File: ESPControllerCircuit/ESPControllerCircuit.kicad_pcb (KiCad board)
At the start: 2 copper layers, 75 x 30 mm, 25 parts, among them J1 Input, J2 Input, J3 Input, J4 Input, J5 Optional, U1 WeMos_mini, U2 HMHA2801, U3 PCF8574T/3,518

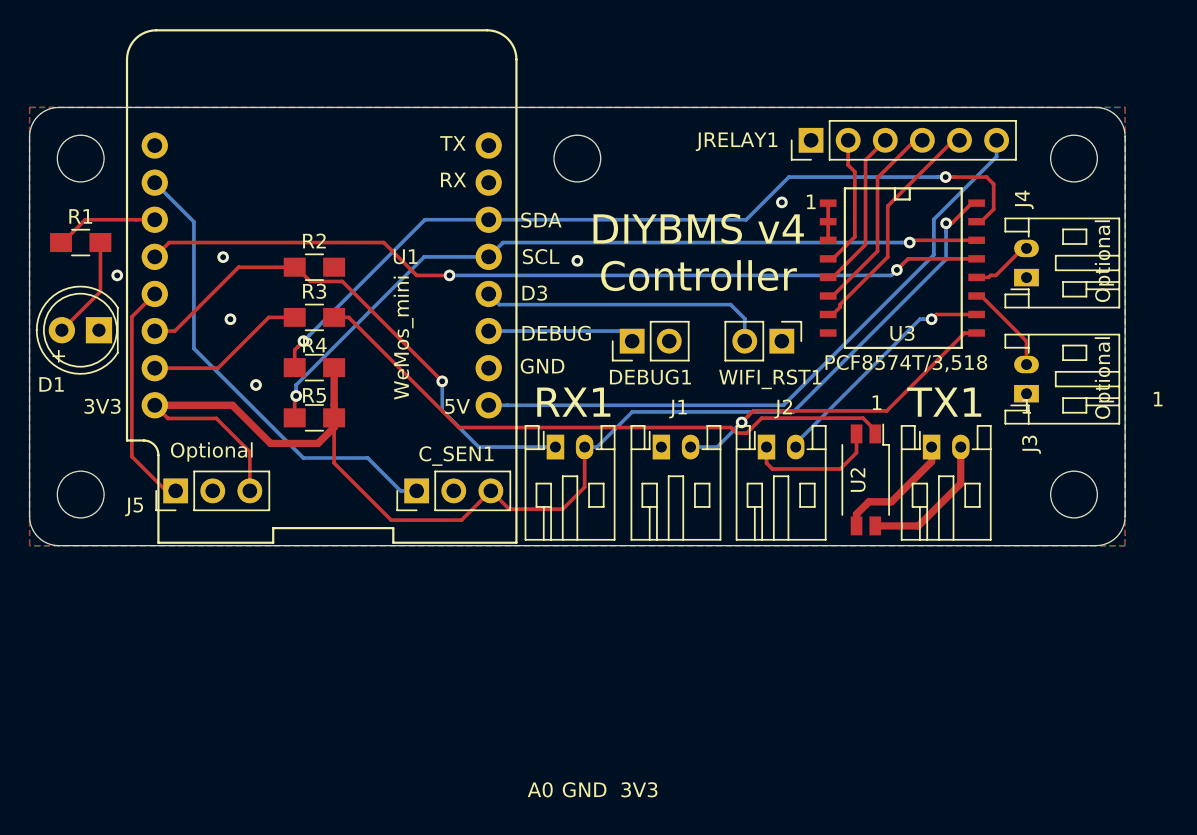
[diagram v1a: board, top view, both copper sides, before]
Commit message: Fix for issue #44
Enlarge footprint for PCF8574 to SOIC16-Wide
Swap LED to surface mount
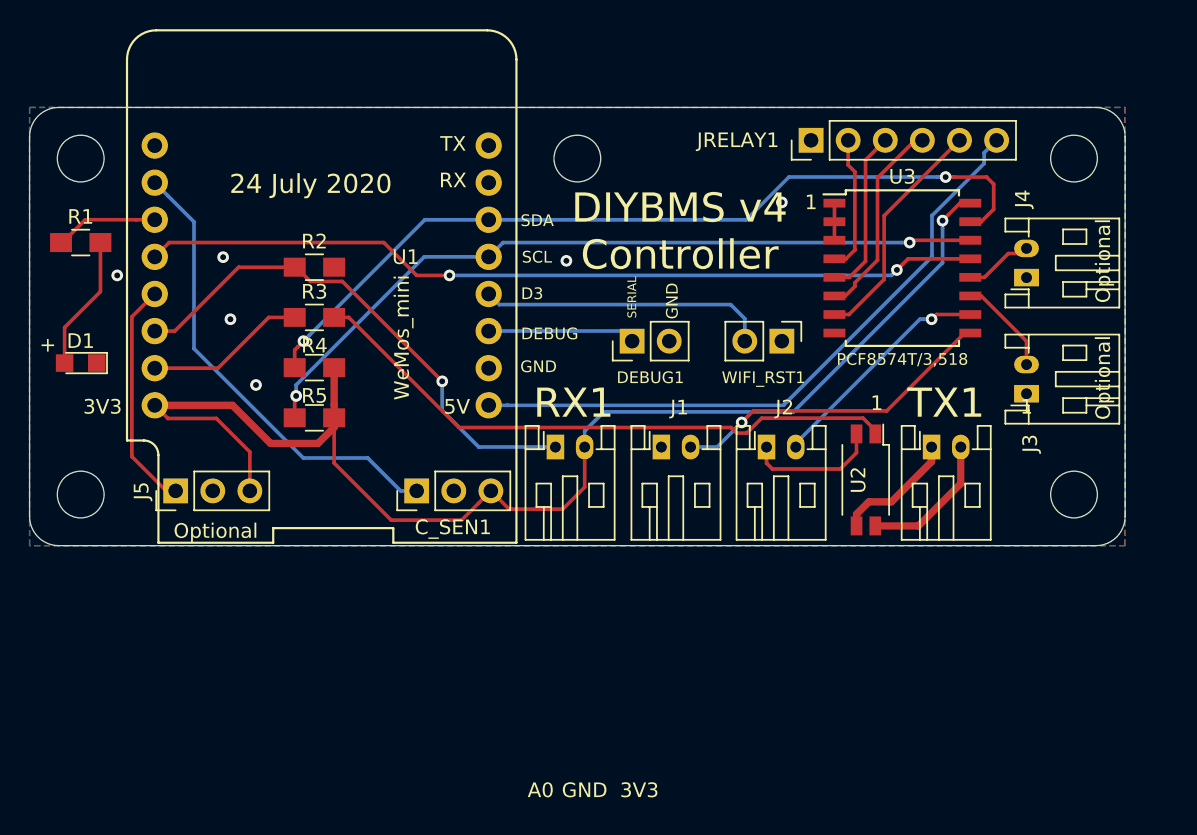
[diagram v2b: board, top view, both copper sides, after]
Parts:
- D1: footprint LEDs:LED_D5.0mm -> LEDs:LED_0805
- U2: value HMHA2801 -> EL3H7(B)(TA)-G
- U3: footprint SMD_Packages:SO-16-W -> Housings_SOIC:SOIC-16W_7.5x10.3mm_Pitch1.27mm
- moved D1 2.57 mm to (76.0, 119.5)
- turned U3 to 0 degrees
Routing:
- net Net-(D1-Pad2): track 7.09 -> 9.26 mm
- net +3V3: track 90.2 -> 91.1 mm
- net Net-(JRELAY1-Pad3): track 11.2 -> 11.9 mm
- net Net-(JRELAY1-Pad2): track 9.25 -> 9.78 mm
- net Net-(JRELAY1-Pad4): track 13.8 -> 14.3 mm
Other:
- board text added: "24 July 2020"
- board text added: "SERIAL"
- board text added: "©2019/2020 Stuart Pittaway"
- board text removed: "7 June 2019"
- board text removed: "©2019 Stuart Pittaway"
